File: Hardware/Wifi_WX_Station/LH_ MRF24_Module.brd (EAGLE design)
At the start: 23.8 x 32.4 mm, 7 parts, among them M1 MRF24WB0MA

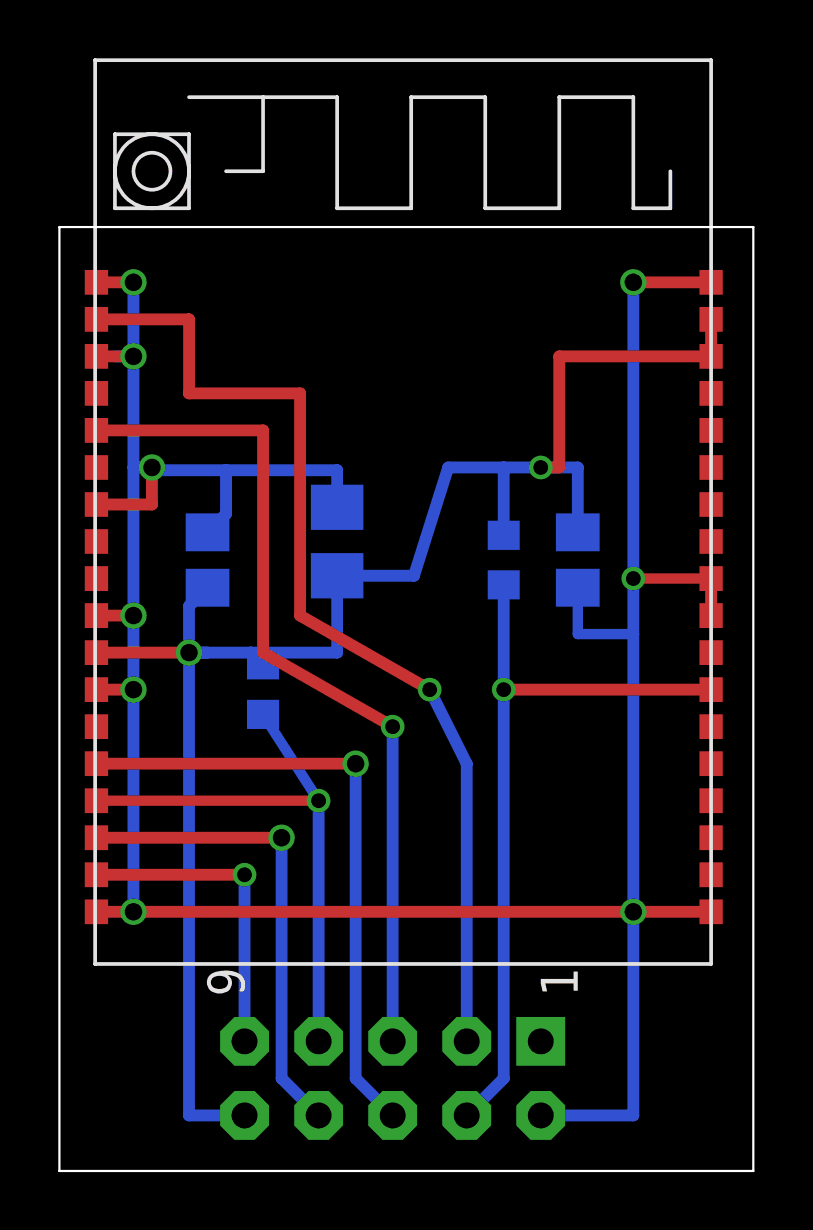
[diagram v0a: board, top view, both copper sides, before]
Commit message: Modified the RF carrier slightly with longer pads for easier soldering.
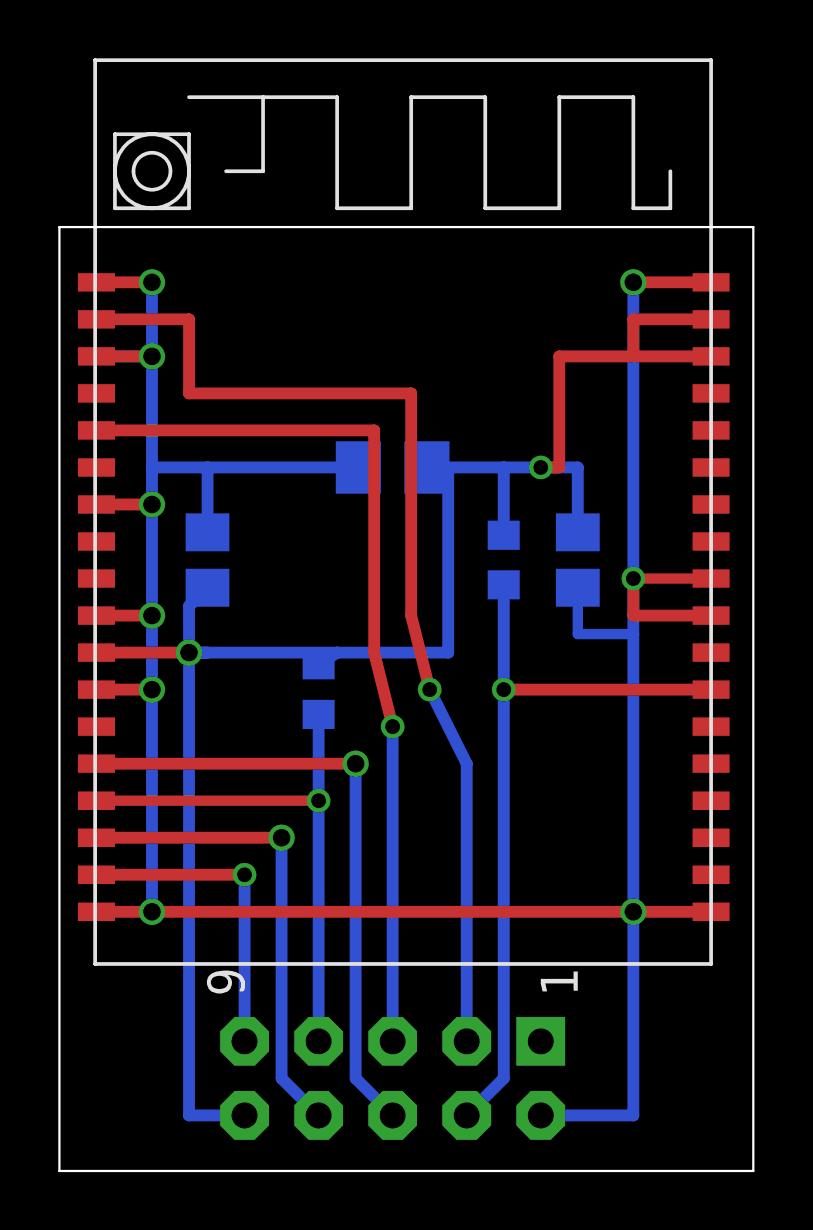
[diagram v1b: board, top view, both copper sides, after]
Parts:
- moved C3 3.17 mm to (32.4, 52.1), turned to 180 degrees
- moved R1 1.90 mm to (29.8, 44.5)
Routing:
- net +3V3: track 58.8 -> 63.4 mm
- net GND: track 104.1 -> 107.3 mm
- net CS_: track 29.2 -> 30.6 mm
- net HIBER: track 34.6 -> 35.9 mm
- net INT_: track 19.4 -> 18.8 mm
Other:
- board text removed: "0.5080 mm / 20.000 mil"
- board text removed: "0.6000 mm / 23.622 mil"
- board text removed: "0.8890 mm / 35.000 mil"
- board text removed: "1 different diameters with default symbols! (10 drills)"
- board text removed: "Date: 1/27/2013 12:12:52 PM"
- board text removed: "Drill legend"
